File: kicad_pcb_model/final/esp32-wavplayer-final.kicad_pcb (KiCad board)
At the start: 2 copper layers, 94 parts, among them J1 BIN+, J2 BIN-, J3 BOUT+, J4 BOUT-, Q1 FS8205A, SW1 RST, SW2 BOOT, U1 TP4056-42-ESOP8, U2 DW01A, U3 PCM5102A

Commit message: Routing PCB
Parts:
- removed C10, C11, C6, C7, C8, C9: C, Capacitor_SMD:C_0805_2012Metric_Pad1.18x1.45mm_HandSolder
- removed J3: BOUT+, Connector_PinHeader_2.54mm:PinHeader_1x01_P2.54mm_Vertical
- removed J4: BOUT-, Connector_PinHeader_2.54mm:PinHeader_1x01_P2.54mm_Vertical
- removed R11: R, Resistor_SMD:R_0805_2012Metric_Pad1.20x1.40mm_HandSolder
- added DC1: C, Capacitor_SMD:C_0603_1608Metric_Pad1.08x0.95mm_HandSolder, F.Cu at (115.4, 149.0)
- added DC2: C, Capacitor_SMD:C_0603_1608Metric_Pad1.08x0.95mm_HandSolder, F.Cu at (115.4, 152.0)
- added DC3: C, Capacitor_SMD:C_0603_1608Metric_Pad1.08x0.95mm_HandSolder, F.Cu at (115.4, 155.0)
- added DC4: C, Capacitor_SMD:C_0603_1608Metric_Pad1.08x0.95mm_HandSolder, F.Cu at (115.4, 158.0)
- added DC5: C, Capacitor_SMD:C_0603_1608Metric_Pad1.08x0.95mm_HandSolder, F.Cu at (115.4, 161.0)
- added DC6: C, Capacitor_SMD:C_0603_1608Metric_Pad1.08x0.95mm_HandSolder, F.Cu at (115.4, 164.1)
- added DC7: C, Capacitor_SMD:C_0603_1608Metric_Pad1.08x0.95mm_HandSolder, F.Cu at (115.4, 167.1)
- added DR3: R, Resistor_SMD:R_0603_1608Metric_Pad0.98x0.95mm_HandSolder, F.Cu at (120.2, 149.0)
- A1, CPU1, USB1: moved to B.Cu
- AC1: renamed from C13; footprint Capacitor_SMD:C_0805_2012Metric_Pad1.18x1.45mm_HandSolder -> Capacitor_SMD:C_0603_1608Metric_Pad1.08x0.95mm_HandSolder
- AC10: renamed from C18; footprint Capacitor_SMD:C_0805_2012Metric_Pad1.18x1.45mm_HandSolder -> Capacitor_SMD:C_0603_1608Metric_Pad1.08x0.95mm_HandSolder
- AC11: renamed from C20; footprint Capacitor_SMD:C_0805_2012Metric_Pad1.18x1.45mm_HandSolder -> Capacitor_SMD:C_0603_1608Metric_Pad1.08x0.95mm_HandSolder
- AC12: renamed from C26; footprint Capacitor_SMD:C_0805_2012Metric_Pad1.18x1.45mm_HandSolder -> Capacitor_SMD:C_0603_1608Metric_Pad1.08x0.95mm_HandSolder
- AC13: renamed from C25; footprint Capacitor_SMD:C_0805_2012Metric_Pad1.18x1.45mm_HandSolder -> Capacitor_SMD:C_0603_1608Metric_Pad1.08x0.95mm_HandSolder
- AC14: renamed from C21; footprint Capacitor_SMD:C_0805_2012Metric_Pad1.18x1.45mm_HandSolder -> Capacitor_SMD:C_0603_1608Metric_Pad1.08x0.95mm_HandSolder
- AC2: renamed from C15; footprint Capacitor_SMD:C_0805_2012Metric_Pad1.18x1.45mm_HandSolder -> Capacitor_SMD:C_0603_1608Metric_Pad1.08x0.95mm_HandSolder
- AC3: renamed from C16; footprint Capacitor_SMD:C_0805_2012Metric_Pad1.18x1.45mm_HandSolder -> Capacitor_SMD:C_0603_1608Metric_Pad1.08x0.95mm_HandSolder
- AC4: renamed from C22; footprint Capacitor_SMD:C_0805_2012Metric_Pad1.18x1.45mm_HandSolder -> Capacitor_SMD:C_0603_1608Metric_Pad1.08x0.95mm_HandSolder
- AC5: renamed from C19; footprint Capacitor_SMD:C_0805_2012Metric_Pad1.18x1.45mm_HandSolder -> Capacitor_SMD:C_0603_1608Metric_Pad1.08x0.95mm_HandSolder
- AC6: renamed from C24; footprint Capacitor_SMD:C_0805_2012Metric_Pad1.18x1.45mm_HandSolder -> Capacitor_SMD:C_0603_1608Metric_Pad1.08x0.95mm_HandSolder
- AC7: renamed from C23; footprint Capacitor_SMD:C_0805_2012Metric_Pad1.18x1.45mm_HandSolder -> Capacitor_SMD:C_0603_1608Metric_Pad1.08x0.95mm_HandSolder
- AC8: renamed from C14; footprint Capacitor_SMD:C_0805_2012Metric_Pad1.18x1.45mm_HandSolder -> Capacitor_SMD:C_0603_1608Metric_Pad1.08x0.95mm_HandSolder
- AC9: renamed from C17; footprint Capacitor_SMD:C_0805_2012Metric_Pad1.18x1.45mm_HandSolder -> Capacitor_SMD:C_0603_1608Metric_Pad1.08x0.95mm_HandSolder
- AD1: renamed from D1; footprint Diode_SMD:D_0805_2012Metric_Pad1.15x1.40mm_HandSolder -> Diode_SMD:D_0603_1608Metric_Pad1.05x0.95mm_HandSolder
- AR1: renamed from R15; footprint Resistor_SMD:R_0805_2012Metric_Pad1.20x1.40mm_HandSolder -> Resistor_SMD:R_0603_1608Metric_Pad0.98x0.95mm_HandSolder
- AR2: renamed from R16; footprint Resistor_SMD:R_0805_2012Metric_Pad1.20x1.40mm_HandSolder -> Resistor_SMD:R_0603_1608Metric_Pad0.98x0.95mm_HandSolder
- AR3: renamed from R14; footprint Resistor_SMD:R_0805_2012Metric_Pad1.20x1.40mm_HandSolder -> Resistor_SMD:R_0603_1608Metric_Pad0.98x0.95mm_HandSolder
- BATPROT1: renamed from U2; moved to B.Cu
- BC1: renamed from C27; footprint Capacitor_SMD:C_0805_2012Metric_Pad1.18x1.45mm_HandSolder -> Capacitor_SMD:C_0603_1608Metric_Pad1.08x0.95mm_HandSolder
- BMFT1: renamed from Q1; moved to B.Cu
- BR1: renamed from R17; footprint Resistor_SMD:R_0805_2012Metric_Pad1.20x1.40mm_HandSolder -> Resistor_SMD:R_0603_1608Metric_Pad0.98x0.95mm_HandSolder
- BR2: renamed from R18; footprint Resistor_SMD:R_0805_2012Metric_Pad1.20x1.40mm_HandSolder -> Resistor_SMD:R_0603_1608Metric_Pad0.98x0.95mm_HandSolder
- BTM1: renamed from U1; footprint Package_SO:SOIC-8-1EP_3.9x4.9mm_P1.27mm_EP2.41x3.3mm_ThermalVias -> Package_SO:SOIC-8_3.9x4.9mm_P1.27mm; moved to B.Cu
- CC1: renamed from UC1; footprint Capacitor_SMD:C_0805_2012Metric_Pad1.18x1.45mm_HandSolder -> Capacitor_SMD:C_0603_1608Metric_Pad1.08x0.95mm_HandSolder; moved to B.Cu
- CC2: renamed from UC2; footprint Capacitor_SMD:C_0805_2012Metric_Pad1.18x1.45mm_HandSolder -> Capacitor_SMD:C_0603_1608Metric_Pad1.08x0.95mm_HandSolder; moved to B.Cu
- CC3: renamed from UC13; footprint Capacitor_SMD:C_0805_2012Metric_Pad1.18x1.45mm_HandSolder -> Capacitor_SMD:C_0603_1608Metric_Pad1.08x0.95mm_HandSolder; moved to B.Cu
- CC4: renamed from C3; footprint Capacitor_SMD:C_0805_2012Metric_Pad1.18x1.45mm_HandSolder -> Capacitor_SMD:C_0603_1608Metric_Pad1.08x0.95mm_HandSolder; moved to B.Cu
- CC5: renamed from C4; footprint Capacitor_SMD:C_0805_2012Metric_Pad1.18x1.45mm_HandSolder -> Capacitor_SMD:C_0603_1608Metric_Pad1.08x0.95mm_HandSolder; moved to B.Cu
- CC6: renamed from C5; footprint Capacitor_SMD:C_0805_2012Metric_Pad1.18x1.45mm_HandSolder -> Capacitor_SMD:C_0603_1608Metric_Pad1.08x0.95mm_HandSolder; moved to B.Cu
- CC7: renamed from UC3; footprint Capacitor_SMD:C_0805_2012Metric_Pad1.18x1.45mm_HandSolder -> Capacitor_SMD:C_0603_1608Metric_Pad1.08x0.95mm_HandSolder; moved to B.Cu
- CC8: renamed from C33; footprint Capacitor_SMD:C_0805_2012Metric_Pad1.18x1.45mm_HandSolder -> Capacitor_SMD:C_0603_1608Metric_Pad1.08x0.95mm_HandSolder; moved to B.Cu
- CC9: renamed from C32; footprint Capacitor_SMD:C_0805_2012Metric_Pad1.18x1.45mm_HandSolder -> Capacitor_SMD:C_0603_1608Metric_Pad1.08x0.95mm_HandSolder; moved to B.Cu
- CR1: renamed from R25; footprint Resistor_SMD:R_0805_2012Metric_Pad1.20x1.40mm_HandSolder -> Resistor_SMD:R_0603_1608Metric_Pad0.98x0.95mm_HandSolder; moved to B.Cu
- CR2: renamed from R26; footprint Resistor_SMD:R_0805_2012Metric_Pad1.20x1.40mm_HandSolder -> Resistor_SMD:R_0603_1608Metric_Pad0.98x0.95mm_HandSolder; moved to B.Cu
- CR3: renamed from R7; footprint Resistor_SMD:R_0805_2012Metric_Pad1.20x1.40mm_HandSolder -> Resistor_SMD:R_0603_1608Metric_Pad0.98x0.95mm_HandSolder; moved to B.Cu
- CR4: renamed from R10; footprint Resistor_SMD:R_0805_2012Metric_Pad1.20x1.40mm_HandSolder -> Resistor_SMD:R_0603_1608Metric_Pad0.98x0.95mm_HandSolder; moved to B.Cu
- D3: value LEDRED -> PWRLED; footprint LED_SMD:LED_0805_2012Metric_Pad1.15x1.40mm_HandSolder -> LED_SMD:LED_0603_1608Metric_Pad1.05x0.95mm_HandSolder
- D4: value LEDBLU -> ONLED; footprint LED_SMD:LED_0805_2012Metric_Pad1.15x1.40mm_HandSolder -> LED_SMD:LED_0603_1608Metric_Pad1.05x0.95mm_HandSolder
- D5: value LED -> CHRGLED; footprint LED_SMD:LED_0805_2012Metric_Pad1.15x1.40mm_HandSolder -> LED_SMD:LED_0603_1608Metric_Pad1.05x0.95mm_HandSolder; moved to B.Cu
- D6: value LED -> STNDLED; footprint LED_SMD:LED_0805_2012Metric_Pad1.15x1.40mm_HandSolder -> LED_SMD:LED_0603_1608Metric_Pad1.05x0.95mm_HandSolder; moved to B.Cu
- DR1: renamed from R12; footprint Resistor_SMD:R_0805_2012Metric_Pad1.20x1.40mm_HandSolder -> Resistor_SMD:R_0603_1608Metric_Pad0.98x0.95mm_HandSolder
- DR2: renamed from R13; footprint Resistor_SMD:R_0805_2012Metric_Pad1.20x1.40mm_HandSolder -> Resistor_SMD:R_0603_1608Metric_Pad0.98x0.95mm_HandSolder
- LR1: renamed from R19; footprint Resistor_SMD:R_0805_2012Metric_Pad1.20x1.40mm_HandSolder -> Resistor_SMD:R_0603_1608Metric_Pad0.98x0.95mm_HandSolder
- LR2: renamed from R20; footprint Resistor_SMD:R_0805_2012Metric_Pad1.20x1.40mm_HandSolder -> Resistor_SMD:R_0603_1608Metric_Pad0.98x0.95mm_HandSolder
- MSD1: footprint Module:Maple_Mini -> Connector_Card:microSD_HC_Hirose_DM3AT-SF-PEJM5; moved to B.Cu
- OC1: renamed from C28; footprint Capacitor_SMD:C_0805_2012Metric_Pad1.18x1.45mm_HandSolder -> Capacitor_SMD:C_0603_1608Metric_Pad1.08x0.95mm_HandSolder
- OC2: renamed from C29; footprint Capacitor_SMD:C_0805_2012Metric_Pad1.18x1.45mm_HandSolder -> Capacitor_SMD:C_0603_1608Metric_Pad1.08x0.95mm_HandSolder
- PC1, PC2: footprint Capacitor_SMD:C_0805_2012Metric_Pad1.18x1.45mm_HandSolder -> Capacitor_SMD:C_0603_1608Metric_Pad1.08x0.95mm_HandSolder; moved to B.Cu
- PC3: renamed from C30; footprint Capacitor_SMD:C_0805_2012Metric_Pad1.18x1.45mm_HandSolder -> Capacitor_SMD:C_0603_1608Metric_Pad1.08x0.95mm_HandSolder; moved to B.Cu
- PC4: renamed from C34; footprint Capacitor_SMD:C_0805_2012Metric_Pad1.18x1.45mm_HandSolder -> Capacitor_SMD:C_0603_1608Metric_Pad1.08x0.95mm_HandSolder; moved to B.Cu
- PC5: renamed from C35; footprint Capacitor_SMD:C_0805_2012Metric_Pad1.18x1.45mm_HandSolder -> Capacitor_SMD:C_0603_1608Metric_Pad1.08x0.95mm_HandSolder; moved to B.Cu
- PD1: renamed from D2; footprint Diode_SMD:D_0805_2012Metric_Pad1.15x1.40mm_HandSolder -> Diode_SMD:D_0603_1608Metric_Pad1.05x0.95mm_HandSolder; moved to B.Cu
- PDVR1: renamed from F1; moved to B.Cu
- PR1: renamed from R5; footprint Resistor_SMD:R_0805_2012Metric_Pad1.20x1.40mm_HandSolder -> Resistor_SMD:R_0603_1608Metric_Pad0.98x0.95mm_HandSolder; moved to B.Cu
- PR2: renamed from R6; footprint Resistor_SMD:R_0805_2012Metric_Pad1.20x1.40mm_HandSolder -> Resistor_SMD:R_0603_1608Metric_Pad0.98x0.95mm_HandSolder; moved to B.Cu
- PR3: renamed from R21; footprint Resistor_SMD:R_0805_2012Metric_Pad1.20x1.40mm_HandSolder -> Resistor_SMD:R_0603_1608Metric_Pad0.98x0.95mm_HandSolder; moved to B.Cu
- PR4: renamed from R22; footprint Resistor_SMD:R_0805_2012Metric_Pad1.20x1.40mm_HandSolder -> Resistor_SMD:R_0603_1608Metric_Pad0.98x0.95mm_HandSolder; moved to B.Cu
- PR5: renamed from R23; footprint Resistor_SMD:R_0805_2012Metric_Pad1.20x1.40mm_HandSolder -> Resistor_SMD:R_0603_1608Metric_Pad0.98x0.95mm_HandSolder; moved to B.Cu
- PR6: renamed from R24; footprint Resistor_SMD:R_0805_2012Metric_Pad1.20x1.40mm_HandSolder -> Resistor_SMD:R_0603_1608Metric_Pad0.98x0.95mm_HandSolder; moved to B.Cu
- PR7: renamed from R27; footprint Resistor_SMD:R_0805_2012Metric_Pad1.20x1.40mm_HandSolder -> Resistor_SMD:R_0603_1608Metric_Pad0.98x0.95mm_HandSolder; moved to B.Cu
- PR8: renamed from R9; footprint Resistor_SMD:R_0805_2012Metric_Pad1.20x1.40mm_HandSolder -> Resistor_SMD:R_0603_1608Metric_Pad0.98x0.95mm_HandSolder; moved to B.Cu
- SC1: renamed from C1; footprint Capacitor_SMD:C_0805_2012Metric_Pad1.18x1.45mm_HandSolder -> Capacitor_SMD:C_0603_1608Metric_Pad1.08x0.95mm_HandSolder
- SC2: renamed from C2; footprint Capacitor_SMD:C_0805_2012Metric_Pad1.18x1.45mm_HandSolder -> Capacitor_SMD:C_0603_1608Metric_Pad1.08x0.95mm_HandSolder
- SR1: renamed from R1; footprint Resistor_SMD:R_0805_2012Metric_Pad1.20x1.40mm_HandSolder -> Resistor_SMD:R_0603_1608Metric_Pad0.98x0.95mm_HandSolder
- SR2: renamed from R2; footprint Resistor_SMD:R_0805_2012Metric_Pad1.20x1.40mm_HandSolder -> Resistor_SMD:R_0603_1608Metric_Pad0.98x0.95mm_HandSolder
- SR3: renamed from R3; footprint Resistor_SMD:R_0805_2012Metric_Pad1.20x1.40mm_HandSolder -> Resistor_SMD:R_0603_1608Metric_Pad0.98x0.95mm_HandSolder
- SR4: renamed from R4; footprint Resistor_SMD:R_0805_2012Metric_Pad1.20x1.40mm_HandSolder -> Resistor_SMD:R_0603_1608Metric_Pad0.98x0.95mm_HandSolder
- moved MSD1 169.7 mm to (18.6, 176.7), turned to 180 degrees
- moved LR2 147.2 mm to (31.6, 82.7)
- moved BR1 147.2 mm to (31.6, 72.1)
- moved BR2 147.2 mm to (31.6, 75.1)
- moved LR1 147.2 mm to (31.6, 78.0)
- moved A1 135.6 mm to (63.0, 56.2), turned to -90 degrees
- moved CR1 133.9 mm to (50.5, 88.4), turned to -90 degrees
- moved PR6 132.6 mm to (59.0, 115.6), turned to -90 degrees
- moved CR2 131.6 mm to (52.5, 88.4), turned to -90 degrees
- moved CR4 129.0 mm to (50.0, 105.6), turned to -90 degrees
- moved D4 127.6 mm to (18.4, 78.0)
- moved PR5 126.5 mm to (63.0, 105.6), turned to -90 degrees
- moved PR3 126.4 mm to (57.0, 115.6), turned to -90 degrees
- moved PR1 124.2 mm to (48.0, 105.6), turned to 90 degrees
- moved USB1 124.1 mm to (50.5, 113.5), turned to 180 degrees
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- renumbered F3 to AVR1, F2 to AVR2, CO1 to CYOC1
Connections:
- AC4 pad 2: GND -> Earth
- AC5 pad 2: GND -> Earth
- AC6 pad 1: GND -> Earth
- AC7 pad 1: GND -> Earth
- BTM1 pad 5: Net-(J1-Pin_1) -> +3V3
- DB3 pad 5: GND -> Earth
- J1 pad 1: Net-(J1-Pin_1) -> +3V3
- PC4 pad 1: Net-(J1-Pin_1) -> +3V3
- PC5 pad 1: Net-(J1-Pin_1) -> +3V3
- PR7 pad 2: Net-(J1-Pin_1) -> +3V3
- U3 pad 12: GND -> Earth
- U3 pad 19: GND -> Earth
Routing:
- net Earth: track 0.00 -> 87.5 mm
- net +3V3: track 0.00 -> 66.1 mm
- net Net-(BTM1-CE): track 0.00 -> 35.1 mm
- net Net-(BATPROT1-GND): track 0.00 -> 33.5 mm
- net /VSYS: track 0.00 -> 28.8 mm
- net Net-(PD1-A): track 0.00 -> 14.9 mm
- net Net-(BATPROT1-VCC): track 0.00 -> 11.1 mm
- net Net-(BTM1-~{CHRG}): track 0.00 -> 9.91 mm
- net Net-(BTM1-~{STDBY}): track 0.00 -> 9.06 mm
- net Net-(BATPROT1-OD): track 0.00 -> 6.77 mm
- net Net-(CR3-Pad2): track 0.00 -> 6.00 mm
- net Net-(BATPROT1-OC): track 0.00 -> 5.79 mm
- net (no net): track 0.00 -> 5.61 mm
- net Net-(BTM1-PROG): track 0.00 -> 4.79 mm
- net Net-(CR4-Pad2): track 0.00 -> 4.68 mm
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
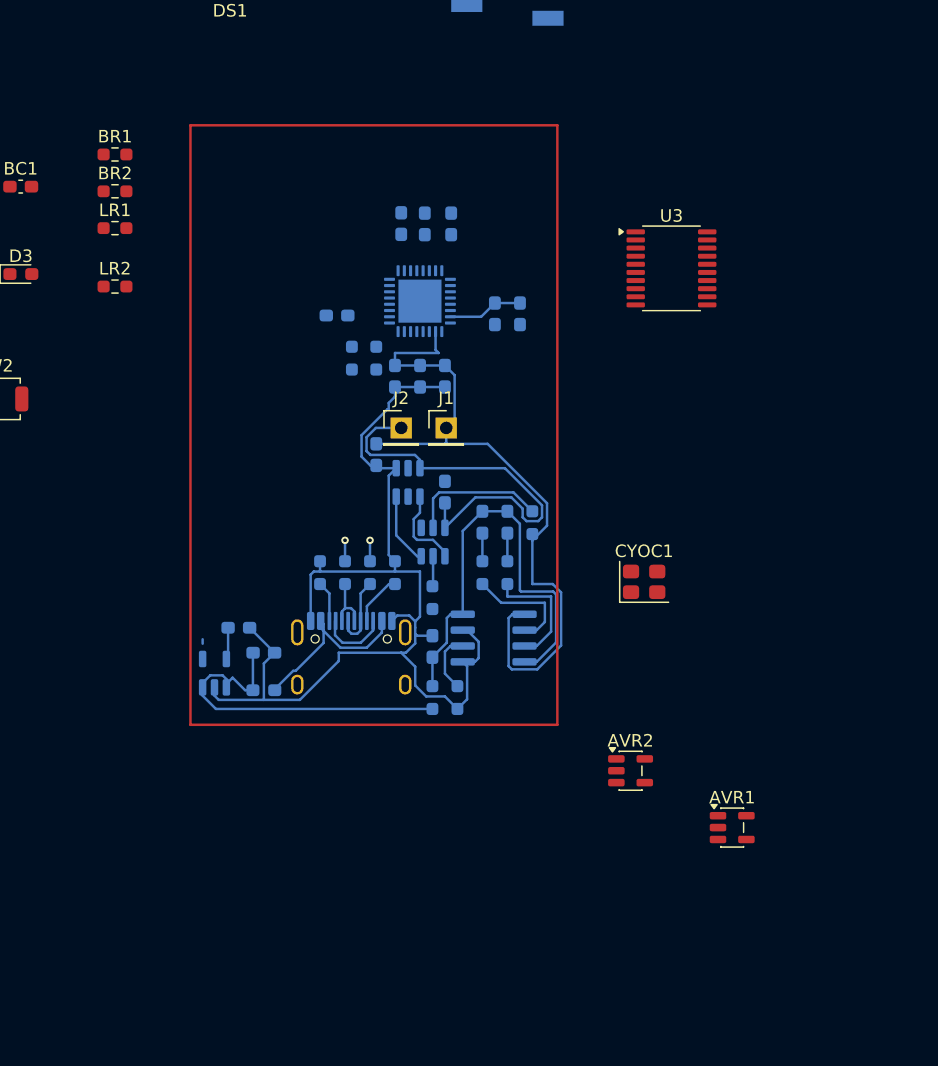
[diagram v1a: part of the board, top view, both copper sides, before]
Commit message: Powerstage redesign
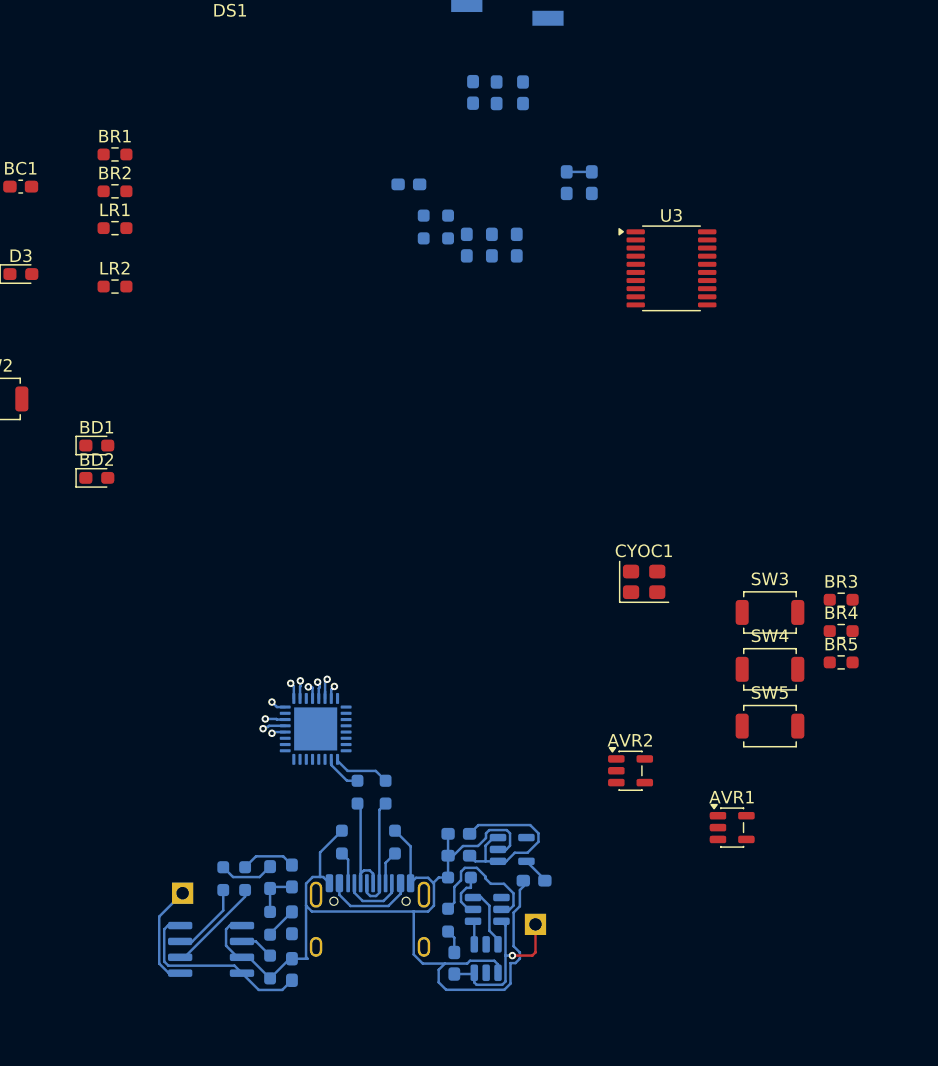
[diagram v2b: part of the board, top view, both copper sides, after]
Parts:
- added BD1: D, Diode_SMD:D_0603_1608Metric_Pad1.05x0.95mm_HandSolder, F.Cu at (30.1, 95.4)
- added BD2: D, Diode_SMD:D_0603_1608Metric_Pad1.05x0.95mm_HandSolder, F.Cu at (30.1, 98.0)
- added BR3: 4.7k, Resistor_SMD:R_0603_1608Metric_Pad0.98x0.95mm_HandSolder, F.Cu at (89.7, 107.8)
- added BR4: 6.8k, Resistor_SMD:R_0603_1608Metric_Pad0.98x0.95mm_HandSolder, F.Cu at (89.7, 110.3)
- added BR5: 15k, Resistor_SMD:R_0603_1608Metric_Pad0.98x0.95mm_HandSolder, F.Cu at (89.7, 112.8)
- added SW3: RIGHT, Button_Switch_SMD:SW_SPST_TS-1088-xR020, F.Cu at (84.0, 108.8)
- added SW4: LEFT, Button_Switch_SMD:SW_SPST_TS-1088-xR020, F.Cu at (84.0, 113.3)
- added SW5: DOWN, Button_Switch_SMD:SW_SPST_TS-1088-xR020, F.Cu at (84.0, 117.9)
- J1, J2: moved to B.Cu
- SW2: value BOOT -> BOOT/UP
- moved J1 42.8 mm to (37.0, 131.2), turned to -90 degrees
- moved J2 41.2 mm to (65.2, 133.8), turned to -90 degrees
- moved BMFT1 38.6 mm to (61.3, 136.5), turned to 90 degrees
- moved PC4 37.7 mm to (58.8, 136.9)
- moved CPU1 35.3 mm to (47.6, 118.1), turned to 0 degrees
- moved D5 34.2 mm to (44.0, 130.0), turned to -90 degrees
- moved BTM1 33.7 mm to (39.3, 135.8), turned to 180 degrees
- moved PR5 33.4 mm to (40.2, 130.1)
- moved PC5 32.8 mm to (59.1, 128.2), turned to 180 degrees
- moved PR7 32.5 mm to (58.2, 133.4)
- moved D6 32.2 mm to (45.8, 129.9), turned to -90 degrees
- moved PC2 31.1 mm to (65.1, 130.2), turned to 180 degrees
- moved PR4 31.0 mm to (42.0, 130.1)
- moved BATPROT1 29.7 mm to (61.4, 132.6), turned to 0 degrees
- moved PC3 28.2 mm to (45.8, 137.4)
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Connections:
- BR2 pad 2: /GPIO9 -> Net-(BD1-A)
- BTM1 pad 5: +3V3 -> Net-(BTM1-BAT)
- CPU1 pad 16: unconnected-(CPU1-GPIO10-Pad16) -> /GPIO10
- CPU1 pad 25: /GPIO18/USB_D- -> /GPIO19/USB_D-
- CPU1 pad 26: /GPIO19/USB_D+ -> /GPIO18/USB_D+
- CPU1 pad 27: unconnected-(CPU1-U0RXD/GPIO20-Pad27) -> /UARTRX
- CPU1 pad 28: unconnected-(CPU1-U0TXD/GPIO21-Pad28) -> /UARTTX
- CPU1 pad 4: unconnected-(CPU1-XTAL_32K_P/ADC1_CH0-Pad4) -> /ANALOG_INPUT
- J1 pad 1: +3V3 -> Net-(BTM1-BAT)
- PC1 pad 1: /VSYS -> Net-(PDVR1-CE)
- PC4 pad 1: +3V3 -> Net-(BTM1-BAT)
- PC5 pad 1: +3V3 -> Net-(PDVR1-CE)
- PDVR1 pad 1: /VSYS -> Net-(PDVR1-CE)
- PDVR1 pad 3: /VSYS -> Net-(PDVR1-CE)
- PR7 pad 2: +3V3 -> Net-(BTM1-BAT)
- SW2 pad 2: /GPIO9 -> Net-(BD1-A)
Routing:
- net +3V3: track 66.1 -> 4.17 mm
- net /VSYS: track 28.8 -> 2.55 mm
- net Net-(BATPROT1-GND): track 33.5 -> 14.8 mm, vias 0 -> 1
- net Net-(BTM1-CE): track 35.1 -> 19.1 mm
- net Net-(PDVR1-CE): track 0.00 -> 15.6 mm
- net Net-(BTM1-BAT): track 0.00 -> 10.3 mm
- net Net-(PD1-A): track 14.9 -> 7.45 mm
- net Net-(BATPROT1-OD): track 6.77 -> 1.89 mm
- net Net-(CR4-Pad2): track 4.68 -> 9.22 mm
- net Net-(BTM1-~{CHRG}): track 9.91 -> 6.12 mm
- net Net-(CR3-Pad2): track 6.00 -> 9.32 mm
- net /GPIO19/USB_D-: track 1.67 -> 4.63 mm, vias 1 -> 0
- net Earth: track 87.5 -> 85.0 mm
- net Net-(D5-K): track 2.25 -> 4.42 mm
- net Net-(D6-K): track 2.25 -> 4.40 mm
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
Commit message: Routing input and display
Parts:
- SC1, SC2, SR1, SR2, SR3, SR4: moved to B.Cu
- moved DB2 141.5 mm to (37.8, 102.2), turned to 180 degrees
- moved SR1 133.5 mm to (43.2, 111.2), turned to 90 degrees
- moved DR1 130.5 mm to (45.0, 95.5), turned to 180 degrees
- moved SR2 130.2 mm to (45.8, 111.2), turned to 90 degrees
- moved DR2 129.9 mm to (45.0, 93.8), turned to 180 degrees
- moved SR3 126.7 mm to (48.5, 111.2), turned to 90 degrees
- moved SR4 123.7 mm to (50.8, 111.2), turned to 90 degrees
- moved DB1 115.7 mm to (53.5, 108.0), turned to -90 degrees
- moved DC6 106.2 mm to (38.5, 90.9), turned to -90 degrees
- moved AR2 106.1 mm to (80.7, 107.5)
- moved DC5 105.6 mm to (36.5, 90.9), turned to -90 degrees
- moved DB3 102.2 mm to (73.8, 131.1)
- moved DC4 99.2 mm to (44.0, 89.1), turned to 90 degrees
- moved DC7 99.1 mm to (55.2, 88.4), turned to 90 degrees
- moved DC3 98.5 mm to (42.2, 89.1), turned to -90 degrees
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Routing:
- net Earth: track 85.0 -> 254.6 mm, vias 0 -> 3
- net +3V3: track 4.17 -> 155.6 mm, vias 0 -> 3
- net /ANALOG_INPUT: track 1.10 -> 69.6 mm
- net Net-(BD1-A): track 0.00 -> 57.7 mm
- net /GPIO9: track 1.07 -> 33.4 mm
- net /GPIO8: track 1.61 -> 24.0 mm, vias 1 -> 0
- net /CHIP_EN: track 0.00 -> 18.8 mm, vias 0 -> 1
- net /GPIO5: track 1.42 -> 19.0 mm, vias 1 -> 0
- net /GPIO7: track 1.40 -> 17.3 mm
- net /GPIO6: track 1.23 -> 15.9 mm
- net /GPIO4: track 1.32 -> 15.1 mm
- net /XTAL_P: track 0.00 -> 10.3 mm, vias 0 -> 1
- net /XTAL_N: track 0.00 -> 8.00 mm, vias 0 -> 1
- net Net-(DS1-C2P): track 0.00 -> 7.59 mm
- net Net-(DS1-C1N): track 0.00 -> 7.13 mm
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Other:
- board outline added: 32 x 63.8 mm

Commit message: Fixing shiz
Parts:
- removed A1: 3.5mmAudioJack, Connector_Audio:Jack_3.5mm_KoreanHropartsElec_PJ-320D-4A_Horizontal
- removed AC1, AC10, AC3, AC4, AC6, AC8: 0.1uF, Capacitor_SMD:C_0603_1608Metric_Pad1.08x0.95mm_HandSolder
- removed AC11, AC12, AC13, AC14: 2.2uF, Capacitor_SMD:C_0603_1608Metric_Pad1.08x0.95mm_HandSolder
- removed AC2, AC5, AC7, AC9, CC6, PC1, PC2, PC3, PC5: 10uF, Capacitor_SMD:C_0603_1608Metric_Pad1.08x0.95mm_HandSolder
- removed AD1, BD1, BD2, PD1: D, Diode_SMD:D_0603_1608Metric_Pad1.05x0.95mm_HandSolder
- removed AR1, AR2: 470, Resistor_SMD:R_0603_1608Metric_Pad0.98x0.95mm_HandSolder
- removed AR3, PR4, PR5, PR6: 1k, Resistor_SMD:R_0603_1608Metric_Pad0.98x0.95mm_HandSolder
- removed AVR1, AVR2, PDVR1: ME6211C33M5, Package_TO_SOT_SMD:SOT-23-5
- removed BATPROT1: DW01A, Package_TO_SOT_SMD:SOT-23-6
- removed BC1, CC3, CC4, PC4, SC1: 100nF, Capacitor_SMD:C_0603_1608Metric_Pad1.08x0.95mm_HandSolder
- removed BMFT1: FS8205A, Package_TO_SOT_SMD:SOT-23-6
- removed BR1, BR2, CR1, CR2, SR1, SR2, SR3, SR4: 10k, Resistor_SMD:R_0603_1608Metric_Pad0.98x0.95mm_HandSolder
- removed BR3: 4.7k, Resistor_SMD:R_0603_1608Metric_Pad0.98x0.95mm_HandSolder
- removed BR4: 6.8k, Resistor_SMD:R_0603_1608Metric_Pad0.98x0.95mm_HandSolder
- removed BR5: 15k, Resistor_SMD:R_0603_1608Metric_Pad0.98x0.95mm_HandSolder
- removed BTM1: TP4056-42-ESOP8, Package_SO:SOIC-8_3.9x4.9mm_P1.27mm
- removed C12: C, Capacitor_SMD:C_0805_2012Metric_Pad1.18x1.45mm_HandSolder
- removed CC1, CC2, CC5, CC7: 1uF, Capacitor_SMD:C_0603_1608Metric_Pad1.08x0.95mm_HandSolder
- removed CC8, CC9, SC2: 10nF, Capacitor_SMD:C_0603_1608Metric_Pad1.08x0.95mm_HandSolder
- removed CPU1: ESP32-C3, Package_DFN_QFN:QFN-32-1EP_5x5mm_P0.5mm_EP3.45x3.45mm
- removed CR3, CR4: 22R, Resistor_SMD:R_0603_1608Metric_Pad0.98x0.95mm_HandSolder
- removed CYOC1: 3225-40m, Oscillator:Oscillator_SMD_Abracon_ASE-4Pin_3.2x2.5mm
- removed D3: PWRLED, LED_SMD:LED_0603_1608Metric_Pad1.05x0.95mm_HandSolder
- removed D4: ONLED, LED_SMD:LED_0603_1608Metric_Pad1.05x0.95mm_HandSolder
- removed D5: CHRGLED, LED_SMD:LED_0603_1608Metric_Pad1.05x0.95mm_HandSolder
- removed D6: STNDLED, LED_SMD:LED_0603_1608Metric_Pad1.05x0.95mm_HandSolder
- removed DB1: MicroSDDebug, Connector_PinHeader_2.54mm:PinHeader_1x06_P2.54mm_Vertical
- removed DB2: DisplayDebug, Connector_PinHeader_2.54mm:PinHeader_1x04_P2.54mm_Vertical
- removed DB3: PCM5102aDebug, Connector_PinHeader_2.54mm:PinHeader_1x06_P2.54mm_Vertical
- removed DC1, DC2, DC3, DC4, DC5, DC6, DC7: C, Capacitor_SMD:C_0603_1608Metric_Pad1.08x0.95mm_HandSolder
- removed DR1, DR2, DR3: R, Resistor_SMD:R_0603_1608Metric_Pad0.98x0.95mm_HandSolder
- removed DS1: Wisevision X096-2864KSWPG01-H30, Display:OLED-128O064D
- removed J1: BIN+, Connector_PinHeader_2.54mm:PinHeader_1x01_P2.54mm_Vertical
- removed J2: BIN-, Connector_PinHeader_2.54mm:PinHeader_1x01_P2.54mm_Vertical
- removed LR1, LR2: 5.1k, Resistor_SMD:R_0603_1608Metric_Pad0.98x0.95mm_HandSolder
- removed MSD1: Generic MicroSD, Connector_Card:microSD_HC_Hirose_DM3AT-SF-PEJM5
- removed OC1, OC2: 15pF, Capacitor_SMD:C_0603_1608Metric_Pad1.08x0.95mm_HandSolder
- removed PR1, PR2: 5.1K, Resistor_SMD:R_0603_1608Metric_Pad0.98x0.95mm_HandSolder
- removed PR3: 0.4, Resistor_SMD:R_0603_1608Metric_Pad0.98x0.95mm_HandSolder
- removed PR7: 100, Resistor_SMD:R_0603_1608Metric_Pad0.98x0.95mm_HandSolder
- removed PR8: 1K, Resistor_SMD:R_0603_1608Metric_Pad0.98x0.95mm_HandSolder
- removed SW1: RST, Button_Switch_SMD:SW_SPST_TS-1088-xR020
- removed SW2: BOOT/UP, Button_Switch_SMD:SW_SPST_TS-1088-xR020
- removed SW3: RIGHT, Button_Switch_SMD:SW_SPST_TS-1088-xR020
- removed SW4: LEFT, Button_Switch_SMD:SW_SPST_TS-1088-xR020
- removed SW5: DOWN, Button_Switch_SMD:SW_SPST_TS-1088-xR020
- removed U3: PCM5102A, Package_SO:TSSOP-20_4.4x6.5mm_P0.65mm
- removed USB1: USBC-6Pin, Connector_USB:USB_C_Receptacle_HRO_TYPE-C-31-M-12
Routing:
- net Earth: track 254.6 -> 0.00 mm, vias 3 -> 0
- net +3V3: track 155.6 -> 0.00 mm, vias 3 -> 0
- net /ANALOG_INPUT: track 69.6 -> 0.00 mm, vias 1 -> 0
- net Net-(BD1-A): track 57.7 -> 0.00 mm
- net /GPIO9: track 33.4 -> 0.00 mm, vias 1 -> 0
- net /GPIO8: track 24.0 -> 0.00 mm
- net Net-(BTM1-CE): track 19.1 -> 0.00 mm
- net /GPIO5: track 19.0 -> 0.00 mm
- net /CHIP_EN: track 18.8 -> 0.00 mm, vias 1 -> 0
- net /GPIO7: track 17.3 -> 0.00 mm, vias 1 -> 0
- net /GPIO6: track 15.9 -> 0.00 mm, vias 1 -> 0
- net Net-(PDVR1-CE): track 15.6 -> 0.00 mm
- net /GPIO4: track 15.1 -> 0.00 mm, vias 1 -> 0
- net Net-(BATPROT1-GND): track 14.8 -> 0.00 mm, vias 1 -> 0
- net Net-(BATPROT1-VCC): track 10.7 -> 0.00 mm
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
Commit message: updated wisevision configuration
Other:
- board size 32 x 63.8 mm -> 40 x 49.4 mm
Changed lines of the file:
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@@
 	(gr_rect
 		(start 134.25 69.875)
-		(end 166.25 133.625)
+		(end 174.25 119.25)
 		(stroke
 			(width 0.05)
